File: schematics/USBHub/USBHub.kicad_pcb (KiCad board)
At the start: 2 copper layers, 56.5 x 57.5 mm, 35 parts, among them J1 USB_A_STACKED, J2 USB_A_STACKED, J3 USB_B, J6 Screw_Terminal_01x02, U1 FE1.1, U2 AP2411, Y1 12Mhz

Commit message: Fixed up USBHub symbol and footprint library
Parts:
- U1: footprint MiSTer-G3:FE1_1_QFP48 -> USBHub:FE1_1_QFP48
- U2: footprint MiSTer-G3:AP24x1_SO8_HandSolder -> USBHub:AP24x1_SO8_HandSolder

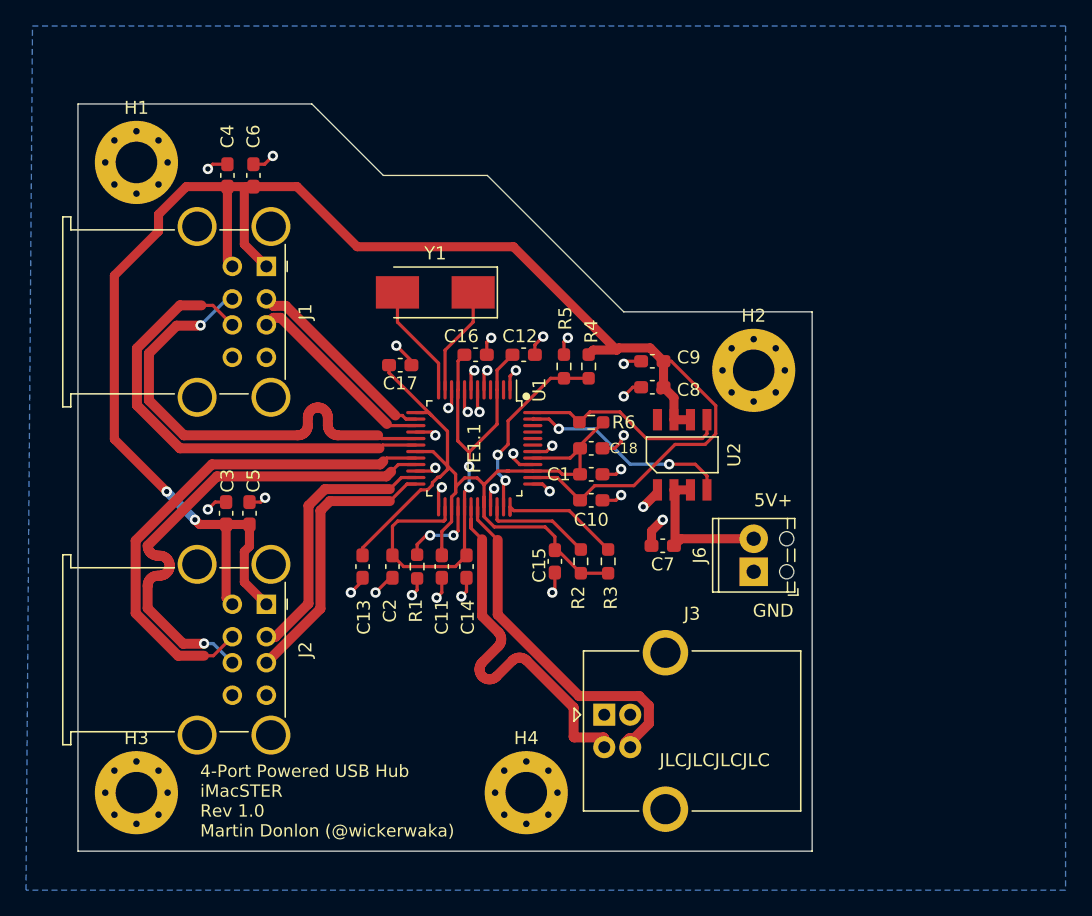
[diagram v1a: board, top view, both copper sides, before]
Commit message: Schematic changes
Reworked Rocky Hills j22 adaptor, removed microphone, added JST headers for speakers, buttons and headphones.
Updated USBHub for FE1.1 5V doesn't go through the current limiting switch
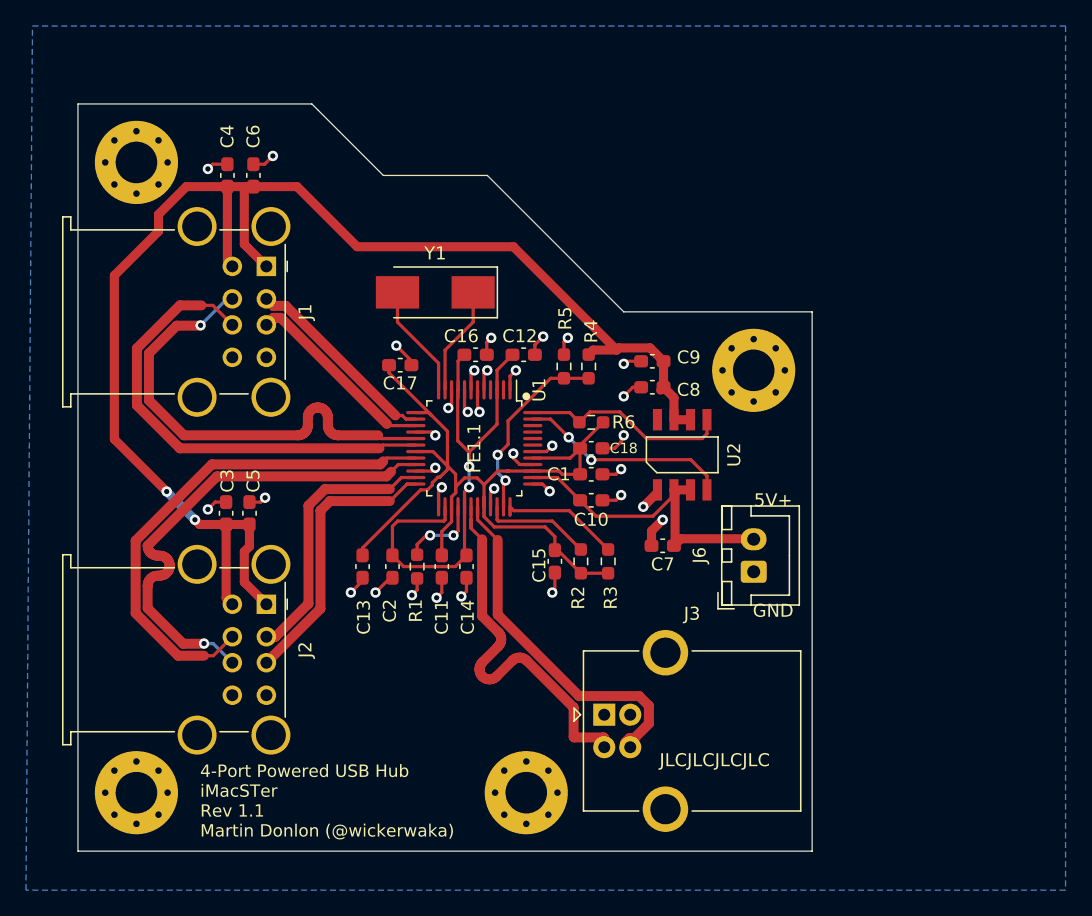
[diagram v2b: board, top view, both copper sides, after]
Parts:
- J6: footprint TerminalBlock_Phoenix:TerminalBlock_Phoenix_MPT-0,5-2-2.54_1x02_P2.54mm_Horizontal -> Connector_JST:JST_XH_B2B-XH-A_1x02_P2.50mm_Vertical
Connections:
- C10 pad 1: VBUS -> VD5
- C7 pad 1: Net-(C7-Pad1) -> VD5
- J6 pad 2: Net-(C7-Pad1) -> VD5
- U1 pad 38: VBUS -> VD5
- U2 pad 2: Net-(C7-Pad1) -> VD5
- U2 pad 3: Net-(C7-Pad1) -> VD5
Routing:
- net VD5: track 0.00 -> 25.2 mm
- net VBUS: track 143.5 -> 119.0 mm
- net Net-(C7-Pad1): track 12.0 -> 0.00 mm
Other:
- board text added: "4-Port Powered USB Hub iMacSTer Rev 1.1 Martin Donlon (@wickerwaka)"
- board text removed: "4-Port Powered USB Hub iMacSTER Rev 1.0 Martin Donlon (@wickerwaka)"

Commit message: USBHub
Added 3d models for usb connectors
Exported a 3d model for the whole hub
Changed the power connector to a horizontal one, not sure if that's what I'll use yet.
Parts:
- J1, J2: footprint Connector_USB:USB_A_Wuerth_61400826021_Horizontal_Stacked -> USBHub:USB_A_Wuerth_61400826021_Horizontal_Stacked
- J3: footprint Connector_USB:USB_B_OST_USB-B1HSxx_Horizontal -> USBHub:USB_B_OST_USB-B1HSxx_Horizontal
- J6: footprint Connector_JST:JST_XH_B2B-XH-A_1x02_P2.50mm_Vertical -> Connector_JST:JST_XH_S2B-XH-A_1x02_P2.50mm_Horizontal

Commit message: Gerber Files
Exported gerber files for all PCBs
Updated main board to version 1.2 with fixes the routing that were bodged into previous version.
Updated to kicad 6
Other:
- net class Default removed
- net class USB removed
